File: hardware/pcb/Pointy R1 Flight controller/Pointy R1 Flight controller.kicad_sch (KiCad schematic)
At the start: 30 parts, among them IC1 TEENSY_4.1, J3 XT60-M, M1 Motor_Servo, M2 Motor_Servo, P1 282837-2, P2 282837-2, P3 282837-2, P4 282837-2, Q1 IRLZ44NSTRLPBF, Q2 IRLZ44NSTRLPBF, Q3 IRLZ44NSTRLPBF, U1 L7805CV, U2 GY-521, U3 MPL3115A2

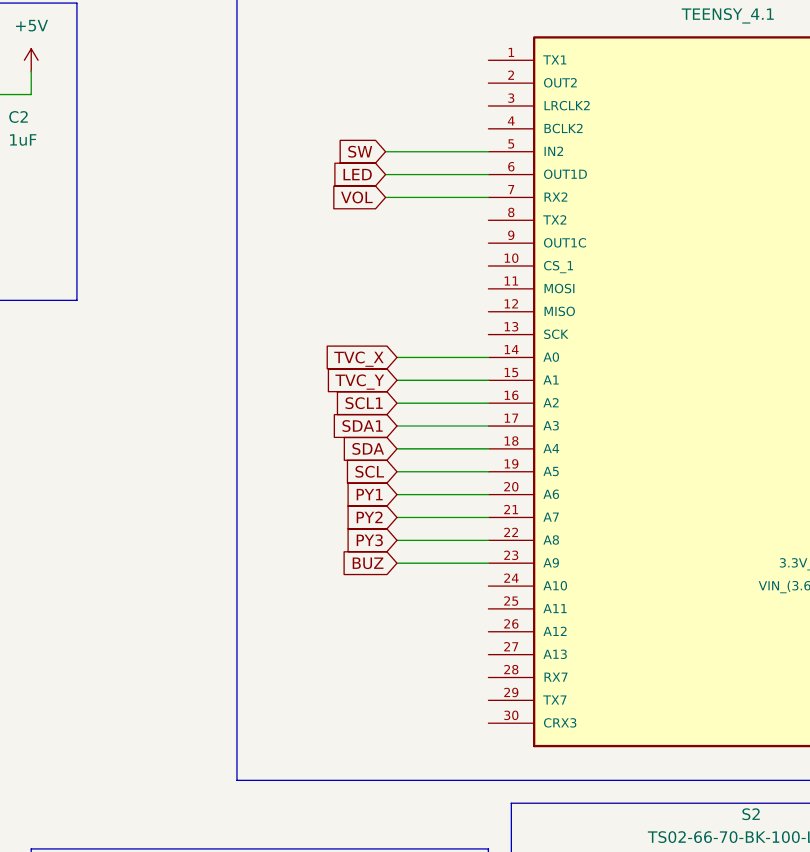
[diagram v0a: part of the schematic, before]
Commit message: Routed majority of traces for all components, excluding minor power management and gnd plane tasks
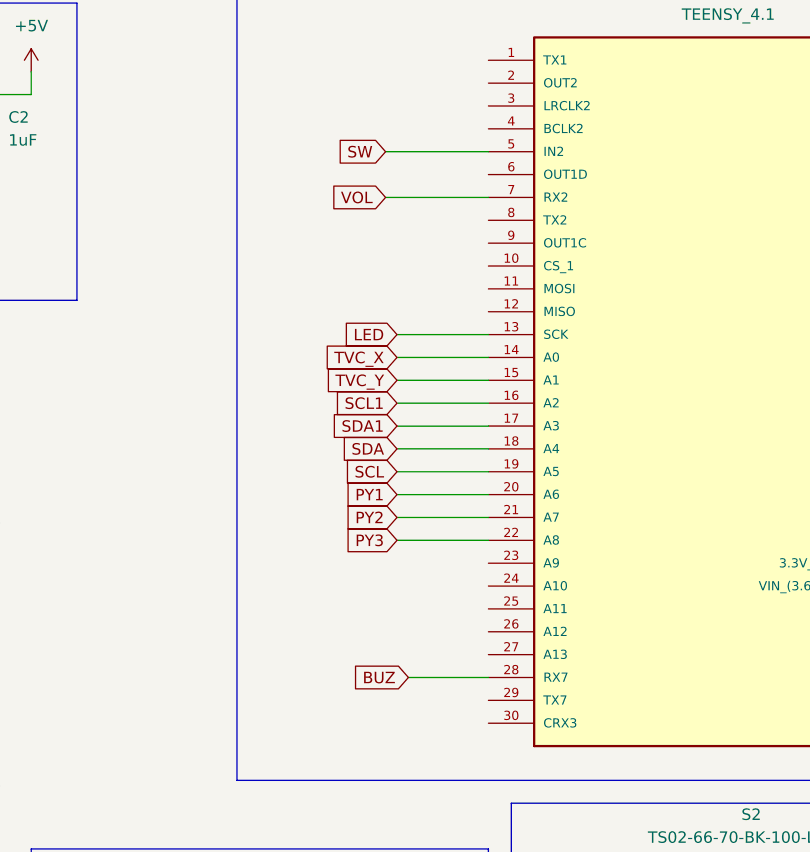
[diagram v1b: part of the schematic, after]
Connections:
- net BUZ: now also IC1.28 (RX7); no longer IC1.23 (A9)
- net LED: now also IC1.13 (SCK); no longer IC1.6 (OUT1D)
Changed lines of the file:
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@@
+	(wire
+		(pts
+			(xy 172.72 52.07) (xy 182.88 52.07)
+		)
+		(stroke
+			(width 0)
+			(type default)
+		)
+	)
 	(wire
 		(pts
@@
 	(wire
 		(pts
+			(xy 173.99 90.17) (xy 182.88 90.17)
+		)
+		(stroke
+			(width 0)
+			(type default)
+		)
+	)
+	(wire
+		(pts
 			(xy 36.83 30.48) (xy 45.72 30.48)
 		)
@@
 	(wire
 		(pts
-			(xy 172.72 77.47) (xy 182.88 77.47)
-		)
-		(stroke
-			(width 0)
-			(type default)
-		)
-	)
-	(wire
-		(pts
 			(xy 166.37 121.92) (xy 166.37 127)
 		)
@@
 		(pts
 			(xy 119.38 66.04) (xy 110.49 66.04)
-		)
-		(stroke
-			(width 0)
-			(type default)
-		)
-	)
-	(wire
-		(pts
-			(xy 171.45 34.29) (xy 182.88 34.29)
 		)
 		(stroke
@@
 	(global_label "LED"
 		(shape input)
-		(at 171.45 34.29 180)
+		(at 172.72 52.07 180)
 		(fields_autoplaced yes)
 		(effects
@@
 		)
 		(property "Intersheetrefs" "${INTERSHEET_REFS}"
-			(at 165.0177 34.29 0)
+			(at 166.2877 52.07 0)
 			(effects
 				(font
@@
 	(global_label "BUZ"
 		(shape input)
-		(at 172.72 77.47 180)
+		(at 173.99 90.17 180)
 		(fields_autoplaced yes)
 		(effects
@@
 		)
 		(property "Intersheetrefs" "${INTERSHEET_REFS}"
-			(at 165.9248 77.47 0)
+			(at 167.1948 90.17 0)
 			(effects
 				(font

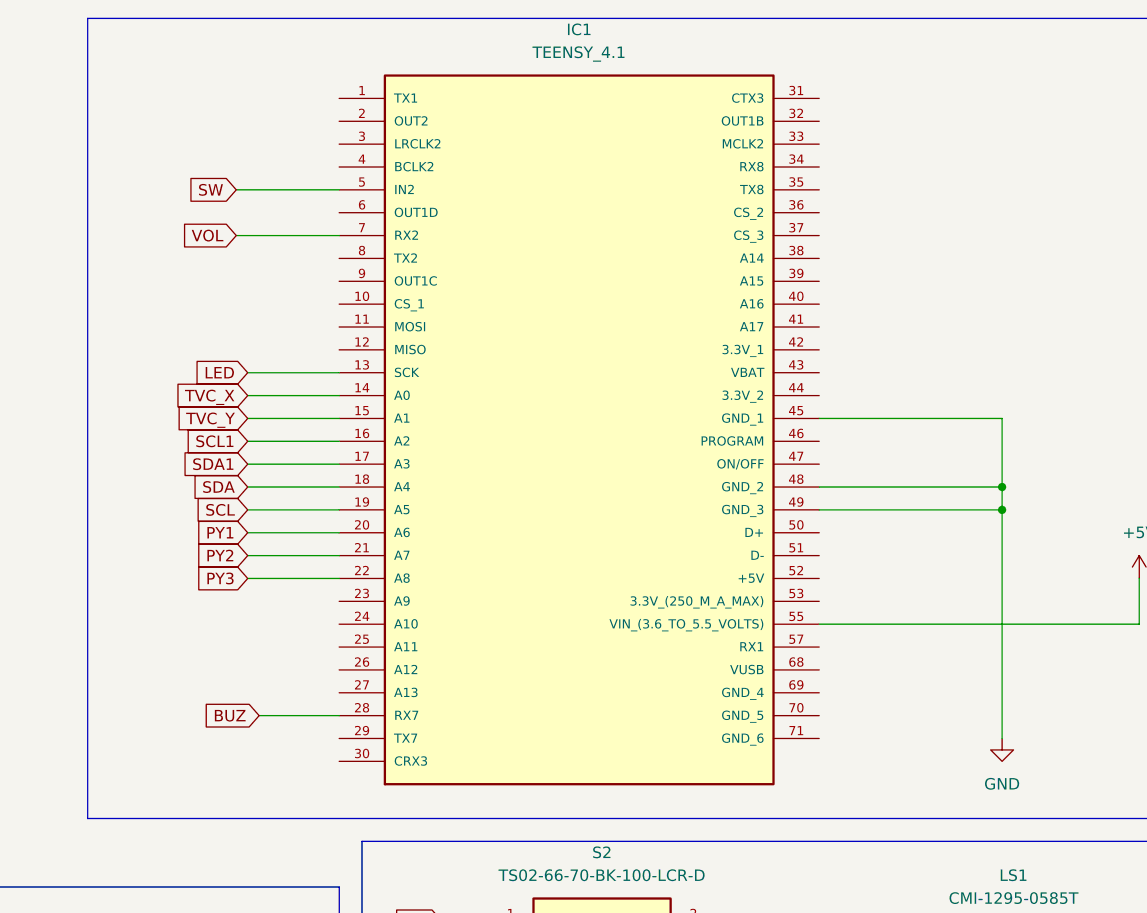
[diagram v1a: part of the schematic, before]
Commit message: Completed routing and added gnd plane, completeting v1 of the PFC - ready for drm
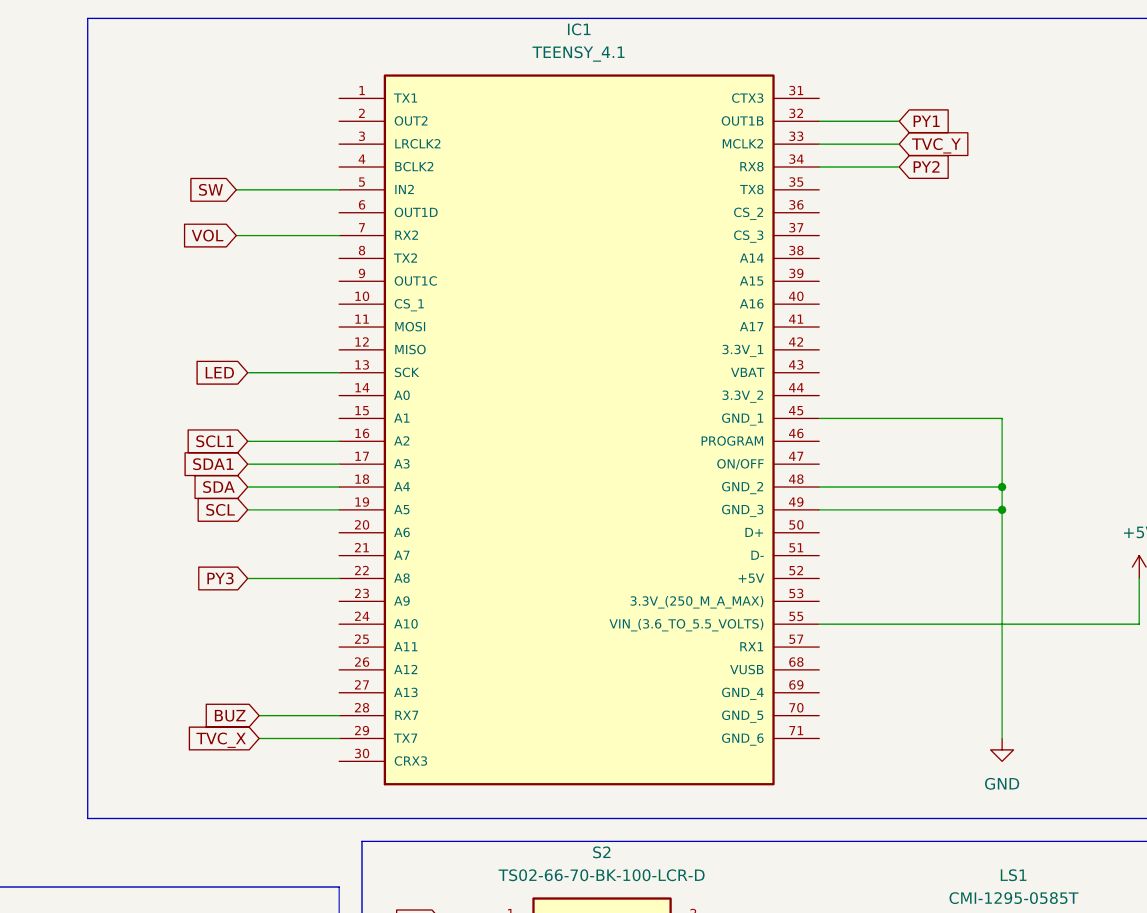
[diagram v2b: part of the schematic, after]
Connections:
- net PY1: now also IC1.32 (OUT1B); no longer IC1.20 (A6)
- net PY2: now also IC1.34 (RX8); no longer IC1.21 (A7)
- net TVC_X: now also IC1.29 (TX7); no longer IC1.14 (A0)
- net TVC_Y: now also IC1.33 (MCLK2); no longer IC1.15 (A1)

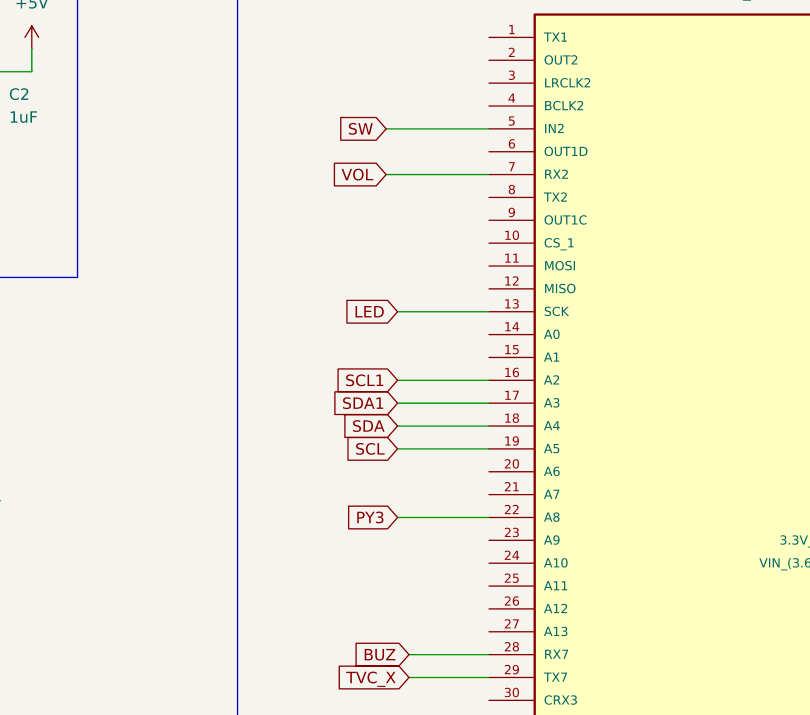
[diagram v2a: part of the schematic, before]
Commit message: Ran DFM + updated pcb accordingly. New gbr files generated
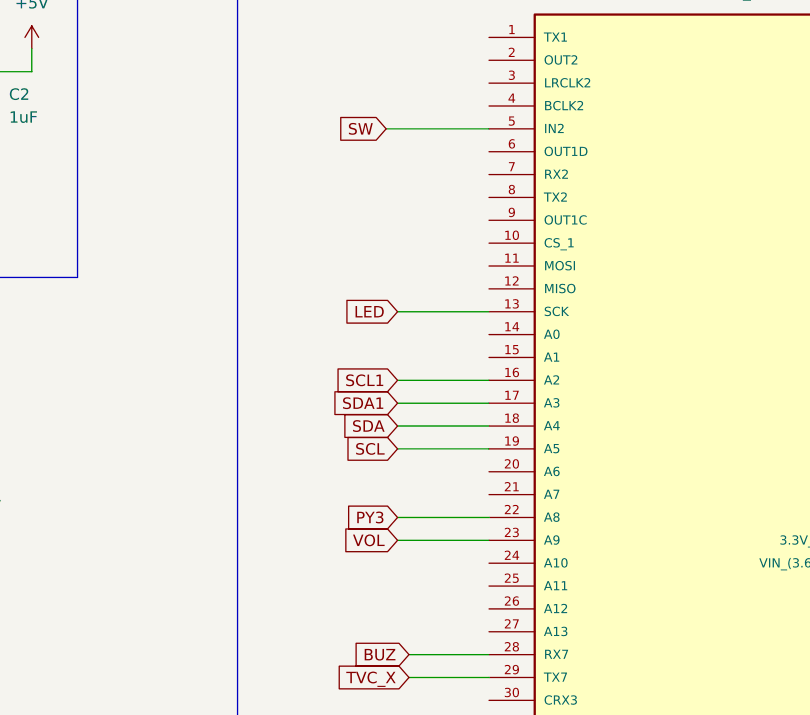
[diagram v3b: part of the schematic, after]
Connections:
- net VOL: now also IC1.23 (A9); no longer IC1.7 (RX2)
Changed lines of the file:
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@@
+	(wire
+		(pts
+			(xy 172.72 77.47) (xy 182.88 77.47)
+		)
+		(stroke
+			(width 0)
+			(type default)
+		)
+	)
 	(wire
 		(pts
@@
 		(pts
 			(xy 53.34 167.64) (xy 66.04 167.64)
-		)
-		(stroke
-			(width 0)
-			(type default)
-		)
-	)
-	(wire
-		(pts
-			(xy 171.45 36.83) (xy 182.88 36.83)
 		)
 		(stroke
@@
 	(global_label "VOL"
 		(shape input)
-		(at 171.45 36.83 180)
+		(at 172.72 77.47 180)
 		(fields_autoplaced yes)
 		(effects
@@
 		)
 		(property "Intersheetrefs" "${INTERSHEET_REFS}"
-			(at 165.0176 36.83 0)
-			(effects
-				(font
+			(at 166.2876 77.47 0)
+			(effects
+				(font
